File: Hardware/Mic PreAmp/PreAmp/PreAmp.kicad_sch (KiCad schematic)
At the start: 5 parts, among them J1 Conn_01x05_Pin, J2 Conn_01x03_Pin, J3 XLR3, U1 TLV2371DBV, U2 INA217AIDWR

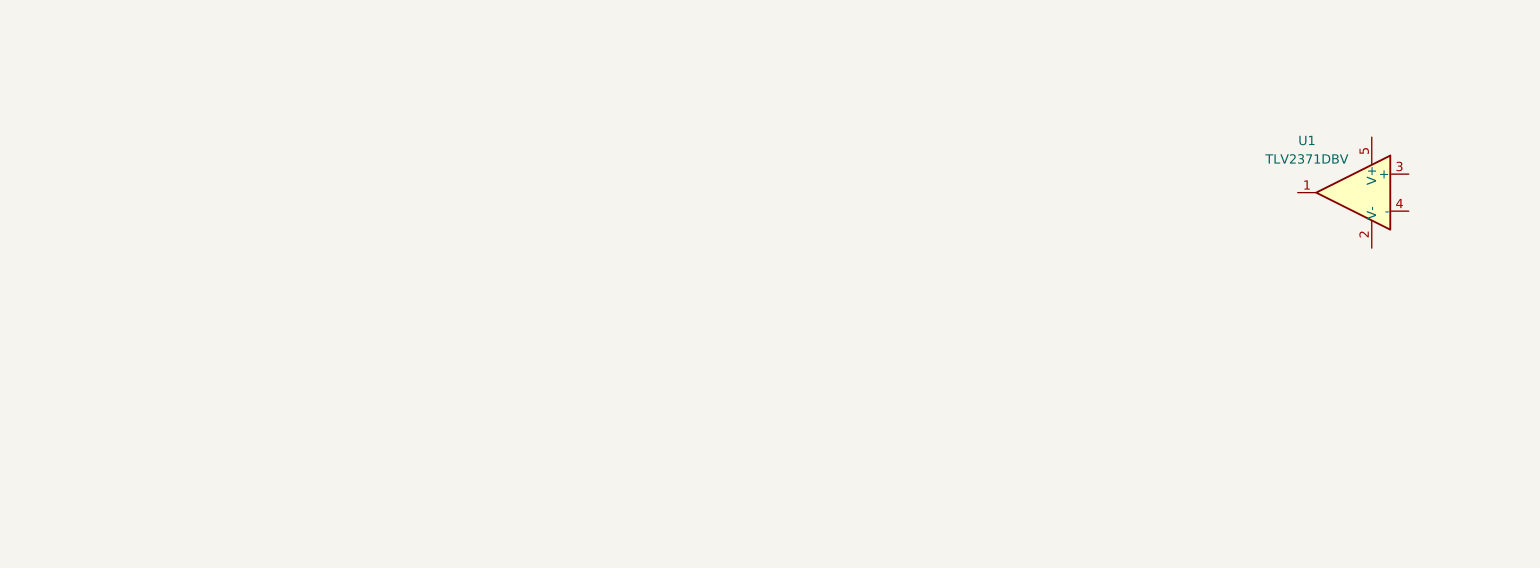
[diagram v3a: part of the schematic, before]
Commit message: Voltage divider circuit
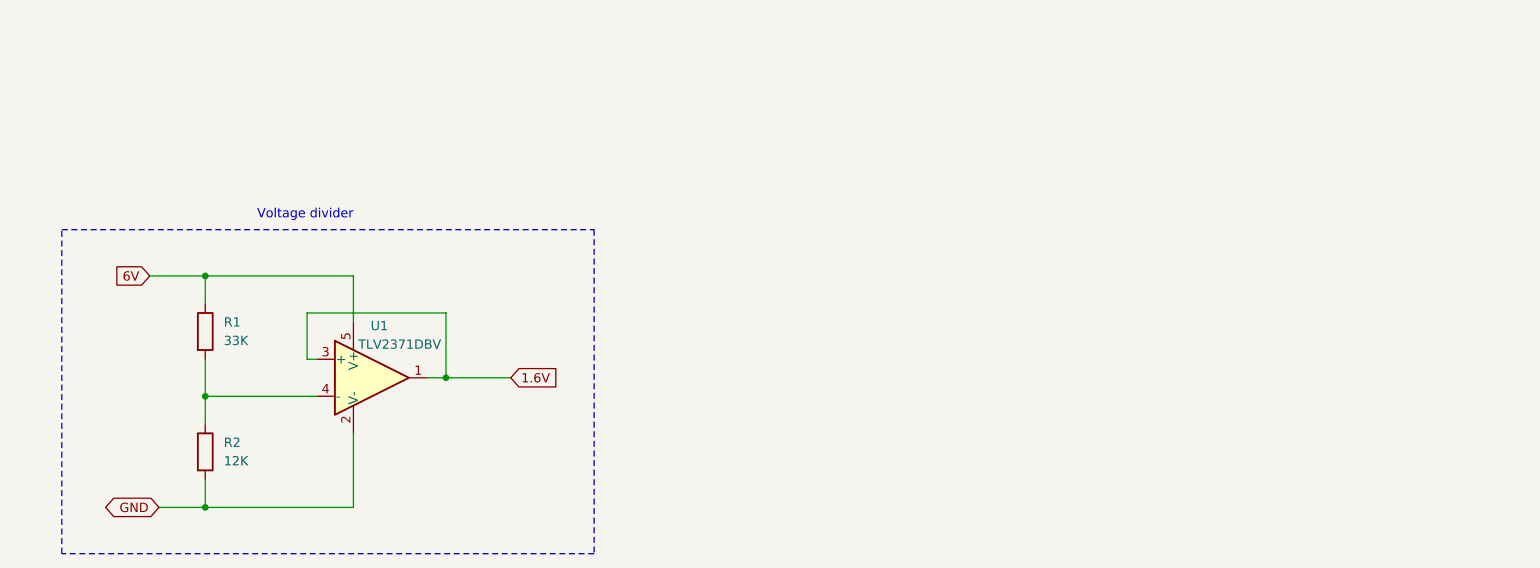
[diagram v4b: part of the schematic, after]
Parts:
- added R1: 33K, symbol Device:R
- added R2: 12K, symbol Device:R
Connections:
- net +6V: now also U1.5 (V+), R1.1
- net GND: now also U1.2 (V-), R2.2
- net 1.6V: now reaches U1.1
- net 1.6V: now also U1.3 (+)
- net at U1.4 (-): now also R1.2, R2.1
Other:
- note added: "Voltage divider"
- moved on the sheet: U1

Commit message: Circuit before V_In
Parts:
- added C1, C2, C3, C4: C, symbol Device:C
- added D1, D2, D3, D4: 1N4148W, Diode_THT:D_DO-35_SOD27_P7.62mm_Horizontal, symbol Diode:1N4148W
- added R3, R4: 33K, symbol Device:R
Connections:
- net +6V: now also U2.13 (V+), C4.1, D1.1 (K), D3.1 (K)
- net -6V: now also U2.7 (V-), C3.1, D2.2 (A), D4.2 (A)
- net Cold: now also C2.1
- net GND: now also U2.10 (REF), C3.2, C4.2, R3.2, R4.2
- net Hot: now also C1.1
- net at U2.4 (VIN-): now also C2.2, D3.2 (A), D4.1 (K), R3.1
- net at U2.5 (VIN+): now also C1.2, D1.2 (A), D2.1 (K), R4.1
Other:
- moved on the sheet: U2

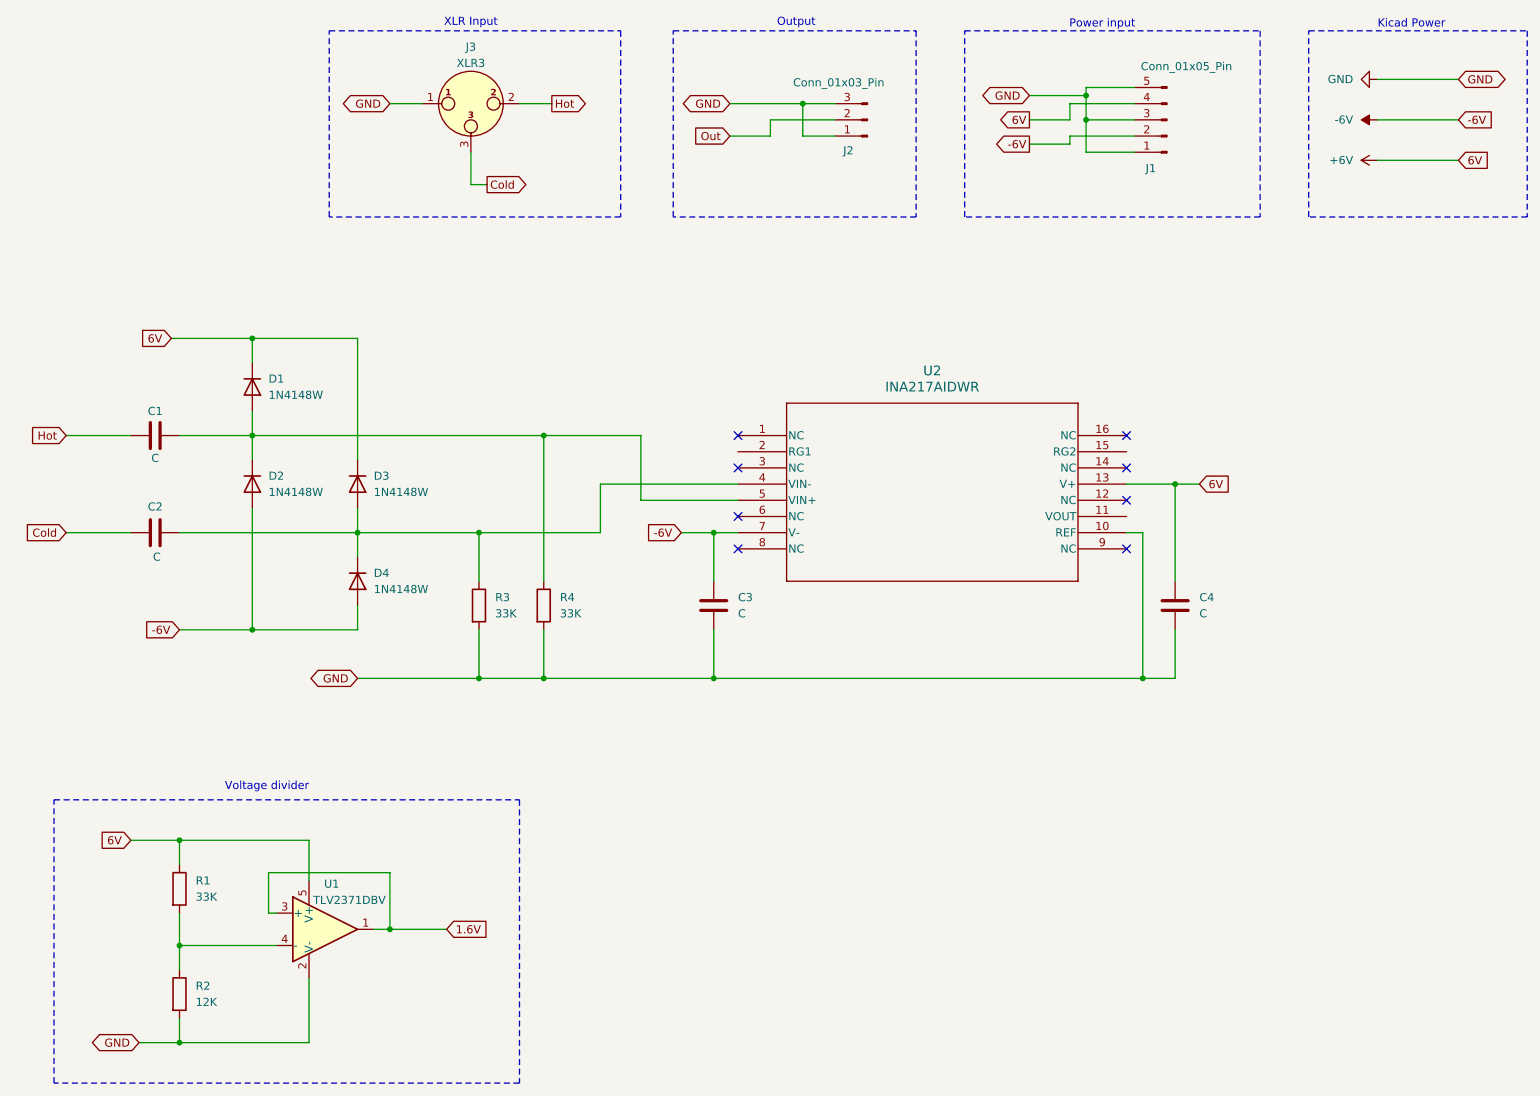
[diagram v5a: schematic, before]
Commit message: Connected REF and Output
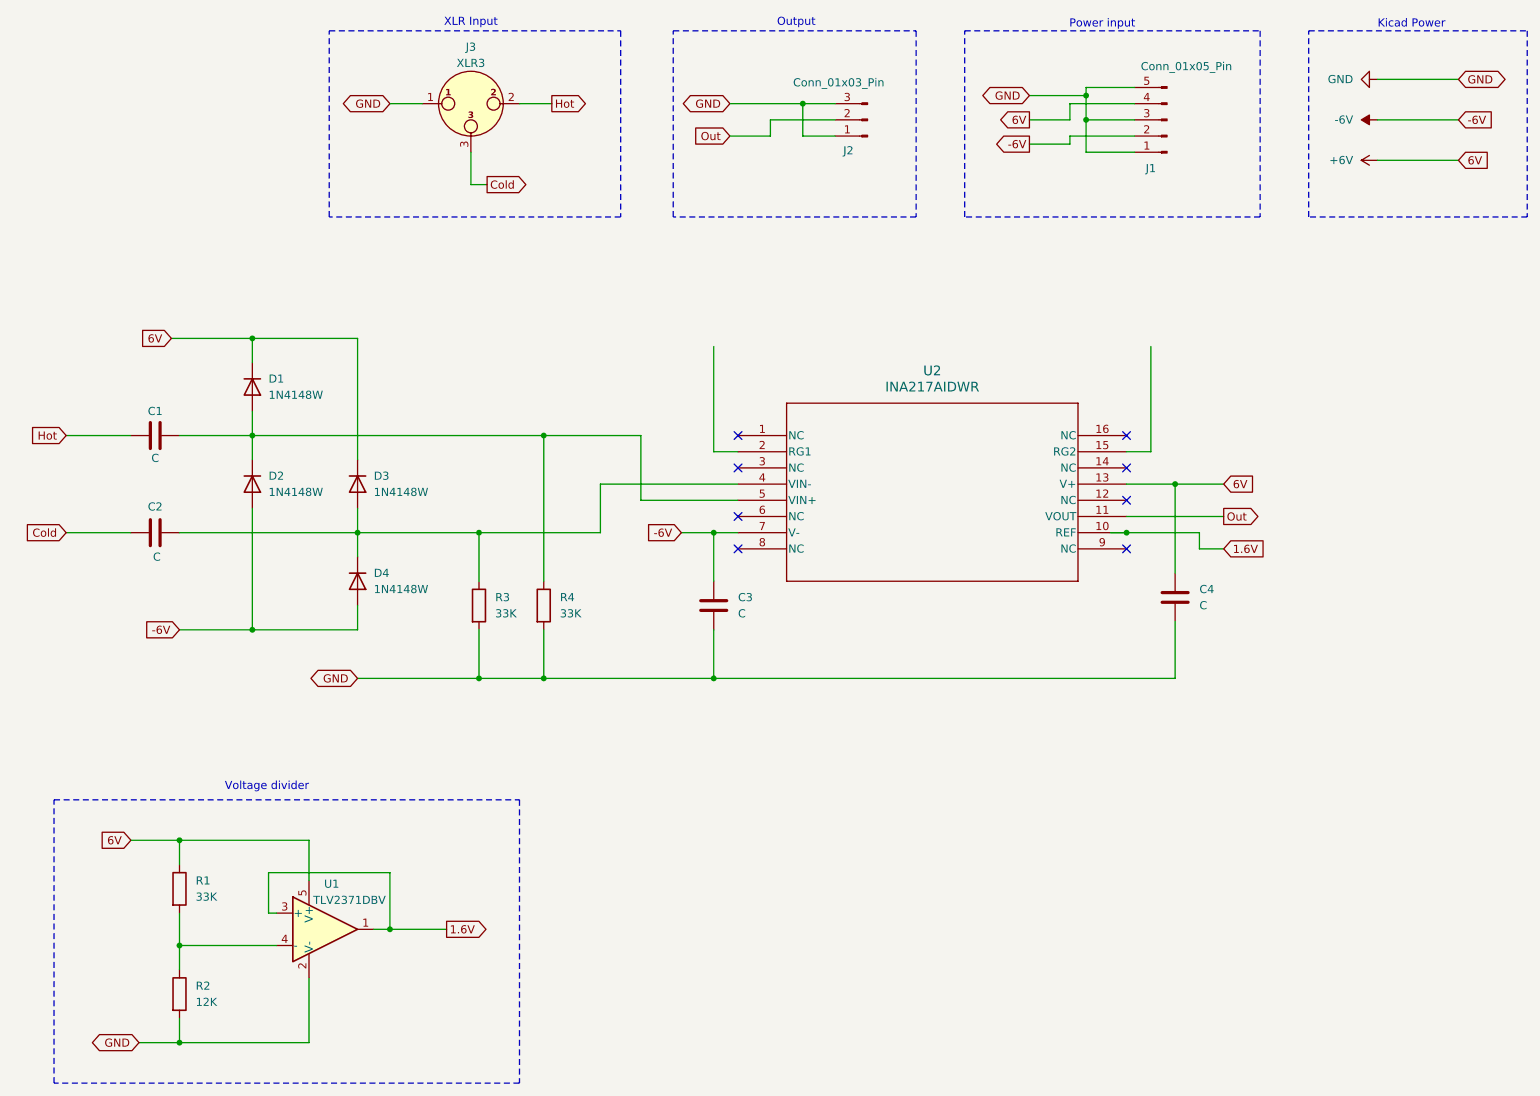
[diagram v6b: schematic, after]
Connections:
- net 1.6V: now also U2.10 (REF)
- net GND: no longer U2.10 (REF)
- net Out: now also U2.11 (VOUT)
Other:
- moved on the sheet: C4
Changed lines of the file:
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@@
-	)
-	(junction
-		(at 213.36 127)
-		(diameter 0)
-		(color 0 0 0 0)
 	)
 	(junction
@@
 	)
 	(junction
+		(at 210.82 104.14)
+		(diameter 0)
+		(color 0 0 0 0)
+	)
+	(junction
 		(at 119.38 88.9)
 		(diameter 0)
@@
 	(wire
 		(pts
-			(xy 146.05 127) (xy 213.36 127)
+			(xy 146.05 91.44) (xy 146.05 74.93)
 		)
 		(stroke
@@
 	(wire
 		(pts
-			(xy 218.44 96.52) (xy 218.44 111.76)
+			(xy 218.44 96.52) (xy 218.44 110.49)
 		)
 		(stroke
@@
 	(wire
 		(pts
+			(xy 149.86 91.44) (xy 146.05 91.44)
+		)
+		(stroke
+			(width 0)
+			(type default)
+		)
+	)
+	(wire
+		(pts
 			(xy 62.23 119.38) (xy 73.66 119.38)
 		)
@@
 	(wire
 		(pts
+			(xy 214.63 74.93) (xy 214.63 91.44)
+		)
+		(stroke
+			(width 0)
+			(type default)
+		)
+	)
+	(wire
+		(pts
 			(xy 90.17 107.95) (xy 90.17 104.14)
 		)
@@
 	(wire
 		(pts
+			(xy 210.82 91.44) (xy 214.63 91.44)
+		)
+		(stroke
+			(width 0)
+			(type default)
+		)
+	)
+	(wire
+		(pts
 			(xy 160.02 36.83) (xy 148.59 36.83)
 		)
@@
 	(wire
 		(pts
-			(xy 218.44 96.52) (xy 222.25 96.52)
+			(xy 218.44 96.52) (xy 226.06 96.52)
 		)
 		(stroke
@@
 	(wire
 		(pts
+			(xy 222.25 106.68) (xy 222.25 104.14)
+		)
+		(stroke
+			(width 0)
+			(type default)
+		)
+	)
+	(wire
+		(pts
 			(xy 160.02 41.91) (xy 160.02 36.83)
 		)
@@
 	(wire
 		(pts
-			(xy 210.82 104.14) (xy 213.36 104.14)
+			(xy 222.25 106.68) (xy 226.06 106.68)
 		)
 		(stroke
@@
 	(wire
 		(pts
-			(xy 213.36 127) (xy 218.44 127)
+			(xy 146.05 127) (xy 218.44 127)
+		)
+		(stroke
+			(width 0)
+			(type default)
+		)
+	)
+	(wire
+		(pts
+			(xy 208.28 104.14) (xy 210.82 104.14)
 		)
 		(stroke
@@
 	(wire
 		(pts
-			(xy 213.36 104.14) (xy 213.36 127)
-		)
-		(stroke
-			(width 0)
-			(type default)
-		)
-	)
-	(wire
-		(pts
 			(xy 90.17 73.66) (xy 90.17 92.71)
 		)
@@
 	(wire
 		(pts
-			(xy 218.44 119.38) (xy 218.44 127)
+			(xy 218.44 118.11) (xy 218.44 127)
 		)
 		(stroke
@@
 	(wire
 		(pts
+			(xy 210.82 101.6) (xy 226.06 101.6)
+		)
+		(stroke
+			(width 0)
+			(type default)
+		)
+	)
+	(wire
+		(pts
 			(xy 201.93 41.91) (xy 201.93 43.18)
 		)
@@
 		(pts
 			(xy 212.09 41.91) (xy 201.93 41.91)
+		)
+		(stroke
+			(width 0)
+			(type default)
+		)
+	)
+	(wire
+		(pts
+			(xy 222.25 104.14) (xy 210.82 104.14)
 		)
 		(stroke
@@
 		)
 	)
+	(global_label "Out"
+		(shape output)
+		(at 226.06 101.6 0)
+		(fields_autoplaced yes)
+		(effects
+			(font
+				(size 1.27 1.27)
+			)
+			(justify left)
+		)
+		(property "Intersheetrefs" "${INTERSHEET_REFS}"
+			(at 232.2504 101.6 0)
+			(effects
+				(font
+					(size 1.27 1.27)
+				)
+				(justify left)
+				(hide yes)
+			)
+		)
+	)
+	(global_label "1.6V"
+		(shape input)
+		(at 226.06 106.68 0)
+		(fields_autoplaced yes)
+		(effects
+			(font
+				(size 1.27 1.27)
+			)
+			(justify left)
+		)
+		(property "Intersheetrefs" "${INTERSHEET_REFS}"
+			(at 233.1576 106.68 0)
+			(effects
+				(font
+					(size 1.27 1.27)
+				)
+				(justify left)
+				(hide yes)
+			)
+		)
+	)
 	(global_label "Cold"
 		(shape output)
@@
 	)
 	(global_label "1.6V"
-		(shape input)
+		(shape output)
 		(at 104.14 166.37 0)
 		(fields_autoplaced yes)
@@
 	(global_label "6V"
 		(shape input)
-		(at 222.25 96.52 0)
+		(at 226.06 96.52 0)
 		(fields_autoplaced yes)
 		(effects
@@
 		)
 		(property "Intersheetrefs" "${INTERSHEET_REFS}"
-			(at 227.5333 96.52 0)
+			(at 231.3433 96.52 0)
 			(effects
 				(font
@@
 	(symbol
 		(lib_id "Device:C")
-		(at 218.44 115.57 0)
+		(at 218.44 114.3 0)
 		(unit 1)
 		(exclude_from_sim no)
@@
 		(fields_autoplaced yes)
 		(property "Reference" "C4"
-			(at 222.25 114.2999 0)
+			(at 222.25 113.0299 0)
 			(effects
 				(font
@@
 		)
 		(property "Value" "C"
-			(at 222.25 116.8399 0)
+			(at 222.25 115.5699 0)
 			(effects
 				(font
@@
 		)
 		(property "Footprint" ""
-			(at 219.4052 119.38 0)
+			(at 219.4052 118.11 0)
 			(effects
 				(font
@@
 		)
 		(property "Datasheet" "~"
-			(at 218.44 115.57 0)
+			(at 218.44 114.3 0)
 			(effects
 				(font
@@
 		)
 		(property "Description" "Unpolarized capacitor"
-			(at 218.44 115.57 0)
-			(effects
-				(font
+			(at 218.44 114.3 0)
+			(effects
+				(font
